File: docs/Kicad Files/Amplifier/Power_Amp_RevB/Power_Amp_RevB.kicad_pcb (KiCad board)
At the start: 2 copper layers, 152.7 x 76.2 mm, 48 parts, among them J1 Speaker, J2 Input Terminals, J3 Power Input, Q1 2N3904, Q10 QD44H8G, Q2 QD45H8G, Q3 2N3904, Q4 2N3906, Q5 QD44H8G, Q6 2N3904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

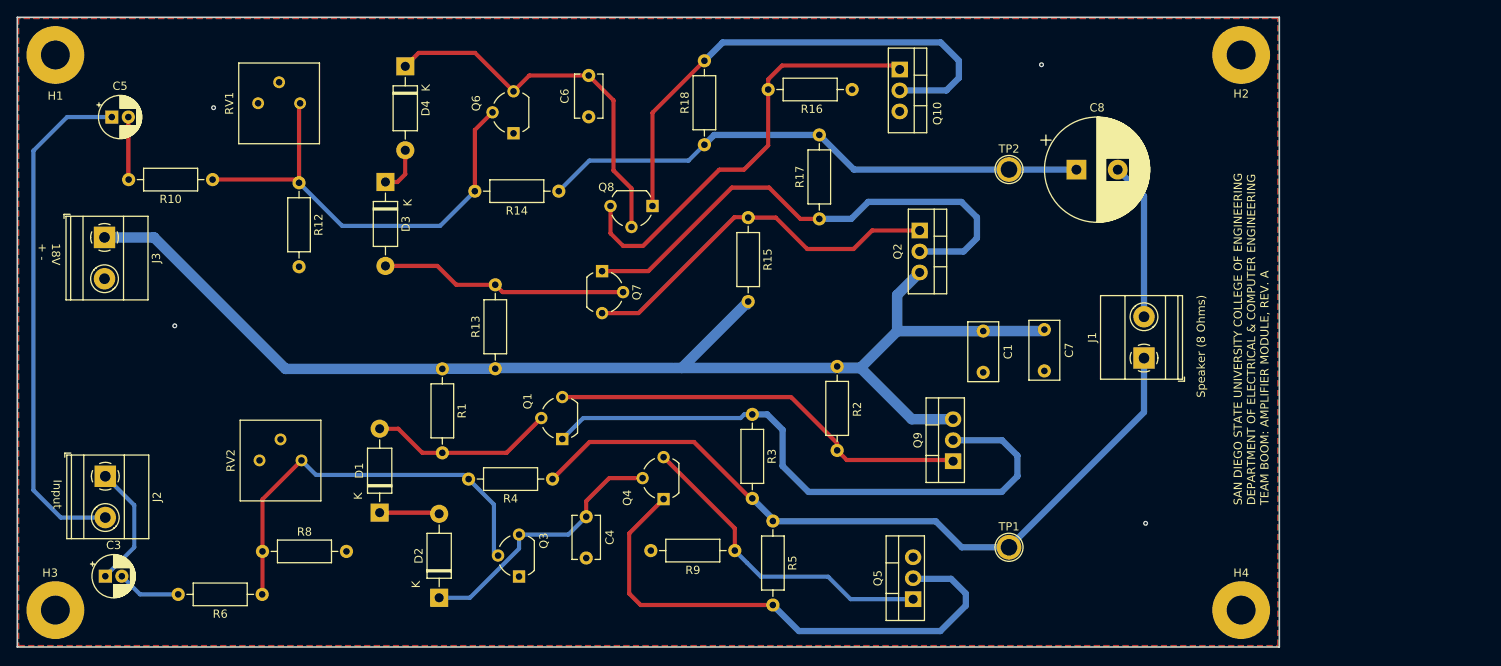
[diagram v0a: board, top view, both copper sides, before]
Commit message: Rev B Update
This update on 10/12/2024 includes a refreshed Amplifier Rev.B design along with a longer PCB length along with courtyards for the power transistors and a logo on the board. AutoCAD .dxf files have been added to the Rev.B folder for future use.
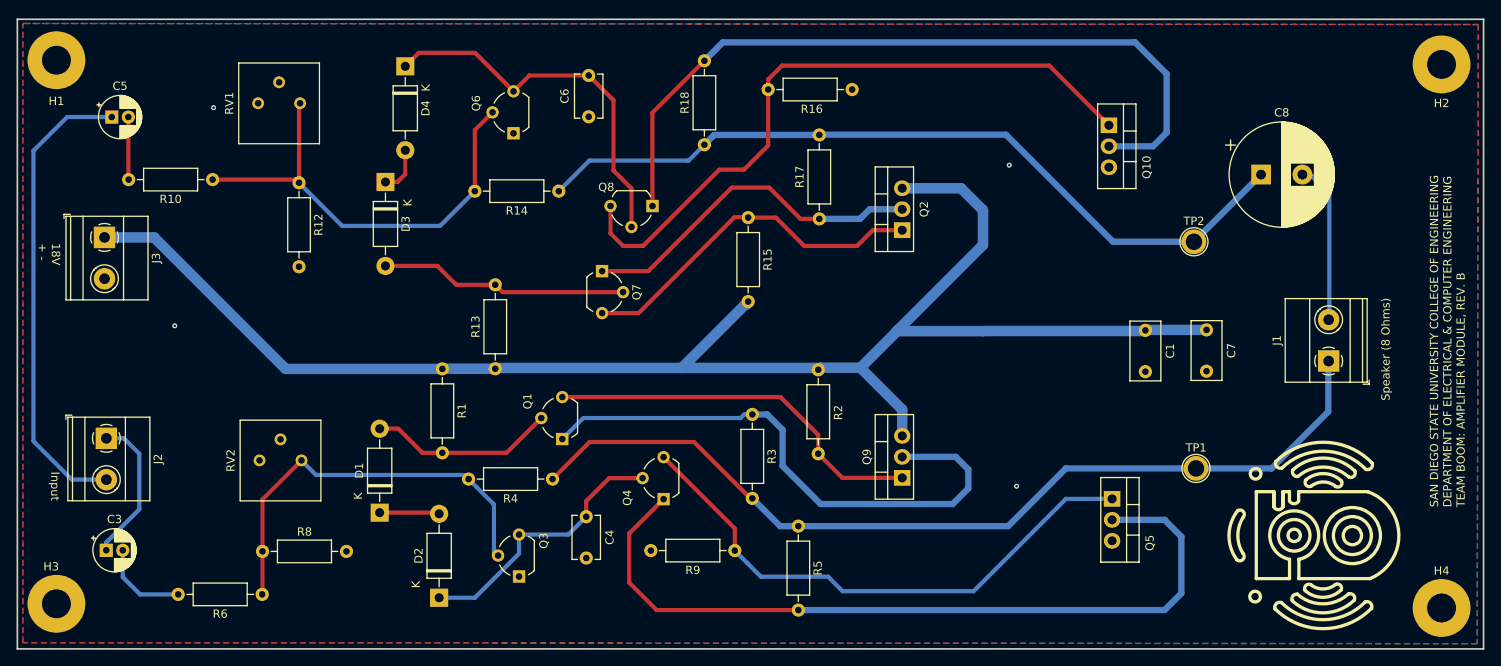
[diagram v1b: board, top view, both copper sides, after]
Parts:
- moved Q5 27.0 mm to (170.9, 120.9), turned to -90 degrees
- moved Q10 26.2 mm to (170.6, 75.7)
- moved TP1 24.6 mm to (181.1, 117.2)
- moved H2 24.3 mm to (210.8, 68.3)
- moved H4 24.3 mm to (210.8, 134.1)
- moved TP2 24.0 mm to (180.8, 89.8)
- moved C8 22.4 mm to (189.0, 81.7)
- moved J1 22.4 mm to (197.2, 104.2)
- moved C1 19.6 mm to (175.0, 100.5)
- moved C7 19.6 mm to (182.4, 100.5)
- moved Q9 6.48 mm to (145.5, 118.4)
- moved J2 4.59 mm to (49.2, 113.6)
- moved C3 3.14 mm to (49.2, 127.1)
- moved R5 3.14 mm to (133.0, 124.2)
- moved R2 2.32 mm to (135.4, 115.4)
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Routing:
- net /18V: track 159.8 -> 207.3 mm
- net Net-(Q4-E): track 65.7 -> 97.0 mm
- net Net-(Q10-C): track 62.7 -> 93.4 mm
- net Net-(C8-Pad1): track 67.2 -> 96.6 mm
- net Net-(Q4-C): track 39.2 -> 67.5 mm
- net Net-(Q10-B): track 52.9 -> 81.0 mm
- net Net-(Q2-C): track 62.9 -> 42.6 mm
- net Net-(J1-Pin_1): track 92.2 -> 111.9 mm
- net Net-(Q1-E): track 74.9 -> 69.4 mm
- net Net-(J2-Pin_2): track 62.3 -> 57.1 mm
- net Net-(Q1-C): track 51.0 -> 46.5 mm
- net Net-(J2-Pin_1): track 15.0 -> 18.1 mm
- net Net-(C3-Pad2): track 7.73 -> 10.8 mm
- net Net-(Q2-B): track 45.8 -> 43.4 mm
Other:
- board size 152.7 x 76.2 mm -> 177.4 x 76.2 mm
- board text added: "SAN DIEGO STATE UNIVERSITY COLLEGE OF ENGINEERING DEPARTMENT OF ELECTRICAL & COMPUTER ENGINEERING TEAM BOOM: AMPLIFIER MODULE, REV. B"
- board text removed: "SAN DIEGO STATE UNIVERSITY COLLEGE OF ENGINEERING DEPARTMENT OF ELECTRICAL & COMPUTER ENGINEERING TEAM BOOM: AMPLIFIER MODULE, REV. A"

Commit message: final changes to both PCBs before review
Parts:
- TP1, TP2: footprint TestPoint:TestPoint_Plated_Hole_D2.0mm -> TestPoint:TestPoint_THTPad_D2.0mm_Drill1.0mm
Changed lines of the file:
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@@
 		)
 	)
-	(footprint "TestPoint:TestPoint_Plated_Hole_D2.0mm"
+	(footprint "TestPoint:TestPoint_THTPad_D2.0mm_Drill1.0mm"
 		(layer "F.Cu")
 		(at 181.102 117.221)
-		(descr "Plated Hole as test Point, diameter 2.0mm")
-		(tags "test point plated hole")
+		(descr "THT pad as test Point, diameter 2.0mm, hole diameter 1.0mm")
+		(tags "test point THT pad")
 		(property "Reference" "TP1"
-			(at 0 -2.498 0)
+			(at 0 -1.998 0)
 			(layer "F.SilkS")
 			(effects
@@
 		)
 		(property "Value" "TestPoint"
-			(at 0 2.45 0)
+			(at 0 2.05 0)
 			(layer "F.Fab")
 			(effects
@@
 			)
 		)
-		(property "Footprint" "TestPoint:TestPoint_Plated_Hole_D2.0mm"
+		(property "Footprint" "TestPoint:TestPoint_THTPad_D2.0mm_Drill1.0mm"
 			(at 0 0 0)
 			(unlocked yes)
@@
 		(fp_circle
 			(center 0 0)
-			(end 0 -1.7)
+			(end 0 1.2)
 			(stroke
 				(width 0.12)
@@
 		(fp_circle
 			(center 0 0)
-			(end 1.8 0)
+			(end 1.5 0)
 			(stroke
 				(width 0.05)
@@
 		)
 		(fp_text user "${REFERENCE}"
-			(at 0 -2.5 0)
+			(at 0 -2 0)
 			(layer "F.Fab")
 			(effects
@@
 		(pad "1" thru_hole circle
 			(at 0 0)
-			(size 3 3)
-			(drill 2)
+			(size 2 2)
+			(drill 1)
 			(layers "*.Cu" "*.Mask")
 			(remove_unused_layers no)
@@
 		)
 	)
-	(footprint "TestPoint:TestPoint_Plated_Hole_D2.0mm"
+	(footprint "TestPoint:TestPoint_THTPad_D2.0mm_Drill1.0mm"
 		(layer "F.Cu")
 		(at 180.848 89.789)
-		(descr "Plated Hole as test Point, diameter 2.0mm")
-		(tags "test point plated hole")
+		(descr "THT pad as test Point, diameter 2.0mm, hole diameter 1.0mm")
+		(tags "test point THT pad")
 		(property "Reference" "TP2"
-			(at 0 -2.498 0)
+			(at 0 -1.998 0)
 			(layer "F.SilkS")
 			(effects
@@
 		)
 		(property "Value" "TestPoint"
-			(at 0 2.45 0)
+			(at 0 2.05 0)
 			(layer "F.Fab")
 			(effects
@@
 			)
 		)
-		(property "Footprint" "TestPoint:TestPoint_Plated_Hole_D2.0mm"
+		(property "Footprint" "TestPoint:TestPoint_THTPad_D2.0mm_Drill1.0mm"
 			(at 0 0 0)
 			(unlocked yes)
@@
 		(fp_circle
 			(center 0 0)
-			(end 0 -1.7)
+			(end 0 1.2)
 			(stroke
 				(width 0.12)
@@
 		(fp_circle
 			(center 0 0)
-			(end 1.8 0)
+			(end 1.5 0)
 			(stroke
 				(width 0.05)
@@
 		)
 		(fp_text user "${REFERENCE}"
-			(at 0 -2.5 0)
+			(at 0 -2 0)
 			(layer "F.Fab")
 			(effects
@@
 		(pad "1" thru_hole circle
 			(at 0 0)
-			(size 3 3)
-			(drill 2)
+			(size 2 2)
+			(drill 1)
 			(layers "*.Cu" "*.Mask")
 			(remove_unused_layers no)
@@
 		(start 197.231 83.947)
 		(end 197.231 99.151)
-		(width 0.508)
+		(width 0.762)
 		(layer "B.Cu")
 		(net 22)
@@
 		(start 194.945 81.661)
 		(end 197.231 83.947)
-		(width 0.508)
+		(width 0.762)
 		(layer "B.Cu")
 		(net 22)
